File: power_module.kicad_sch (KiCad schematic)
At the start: 0 parts

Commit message: schematic: place BMS subcircuit components
25 components placed (no wires yet) in the BMS subcircuit:
  U1   BQ7692003 BMS chip (TSSOP-20)
  BT1-3  three 18650 cells stacked at x=175
  R1-4   cell-tap resistors (100 Ω) for VC0..VC3
  C1-4   cell-tap RC-filter caps (1 nF)
  Q1     dual N-channel MOSFET (FDS9926A symbol; will swap value
         to C353066 in the LCSC pass) for CHG + DSG protection
  R5     0.005 Ω current-sense shunt
  C5     1 µF cap on CAP1 (cell-balance bootstrap)
  C6/C7  REGOUT bypass (1 µF + 100 nF)
  C8/C9  BAT decoupling (10 µF + 100 nF)
  R6-8   I²C SDA/SCL + ALERT pull-ups (10 kΩ)
  R9     NTC bias (10 kΩ)
  TH1    10 kΩ NTC thermistor on TS1
  SW1    user-on/off tactile switch (placeholder; will be wired to
         BMS shutdown via small transistor in a later pass)

Placement was scripted via DynamicSymbolLoader directly rather than
going through 25 sequential MCP calls — same underlying code path,
much faster, and explicitly sequential to dodge the parallel-write
race we saw earlier today.

Component positions are approximately correct but support caps and
pull-up resistors overlap visually; will be cleaned up during wiring.

Wires + footprints + LCSC properties to follow in subsequent commits.

Co-Authored-By: Claude Opus 4.7 <noreply@anthropic.com>
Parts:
- added BT1, BT2, BT3: 18650, symbol Device:Battery_Cell
- added C1, C2, C3, C4: 1nF, symbol Device:C
- added C5, C6: 1uF, symbol Device:C
- added C7, C9: 100nF, symbol Device:C
- added C8: 10uF, symbol Device:C
- added Q1: DUAL_N_FET, symbol Transistor_FET:FDS9926A
- added R1, R2, R3, R4: 100, symbol Device:R
- added R5: 0.005, symbol Device:R
- added R6, R7, R8, R9: 10k, symbol Device:R
- added SW1: OFF, symbol Switch:SW_Push
- added TH1: NTC_10k, symbol Device:Thermistor_NTC
- added U1: BQ7692003, Package_SO:TSSOP-20_4.4x6.5mm_P0.65mm, symbol Battery_Management:BQ76920PW
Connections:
- new net: Q1.7 (D1), Q1.8 (D1)

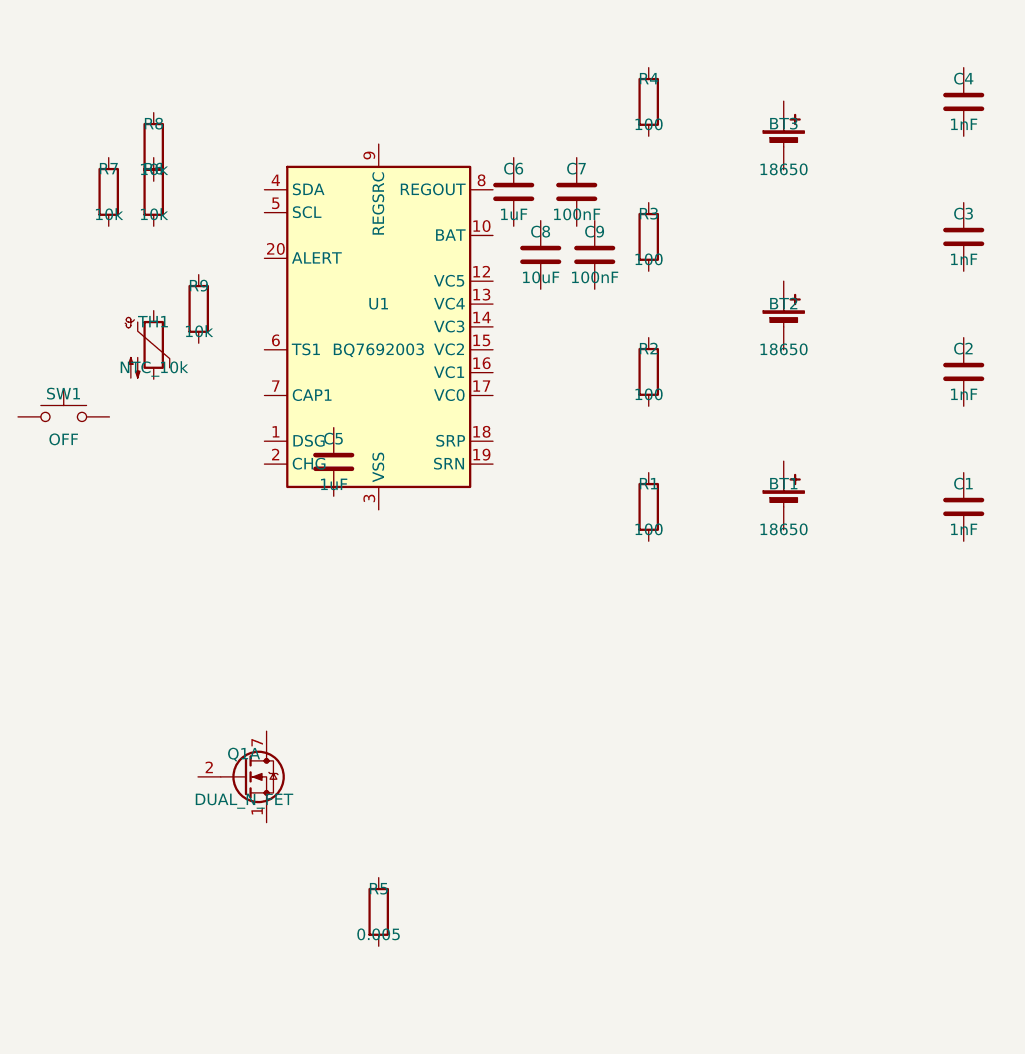
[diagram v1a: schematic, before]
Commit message: schematic: wire BMS subcircuit (cell stack, taps, FETs, signals)
All BMS-side connectivity in place via local net labels:
- Cell stack: BAT+ / CELL2_TOP / CELL1_TOP / BAT-
- Cell taps: VC0..VC3 with R1-R4 + RC caps C1-C4 (3S jumpers tie
  VC4=VC5=VC3 at the BMS pins, post-filter resistor)
- Protection FETs Q1: dual N-FET in back-to-back (drains tied =
  FET_MID, sources to BAT- and SRP, gates to BMS_DSG/BMS_CHG).
  Added Q1 unit 2 (FDS9926A symbol is multi-unit; only unit 1 was
  placed previously).
- Sense resistor R5: SRP at top, GND at bottom = U1.SRN = U1.VSS.
- Support passives: REGOUT (C6/C7), BAT/REGSRC (C8/C9 on BAT+),
  CAP1 (C5).
- Signals: SDA/SCL/ALERT pull-ups to REGOUT (R6/R7/R8); TS1
  thermistor divider (R9 + TH1 to GND).
- PWR_FLAG on BAT+ and GND so ERC accepts the cell stack as a
  power source.
- U1.NC (pin 11) marked no_connect.

ERC clean except for SW1 pins 1/2 (intentional — finalised in
integration step per NOTES.md).

Schematic file reformatted with consistent S-expression indentation
so future diffs stay readable.

Co-Authored-By: Claude Opus 4.7 <noreply@anthropic.com>
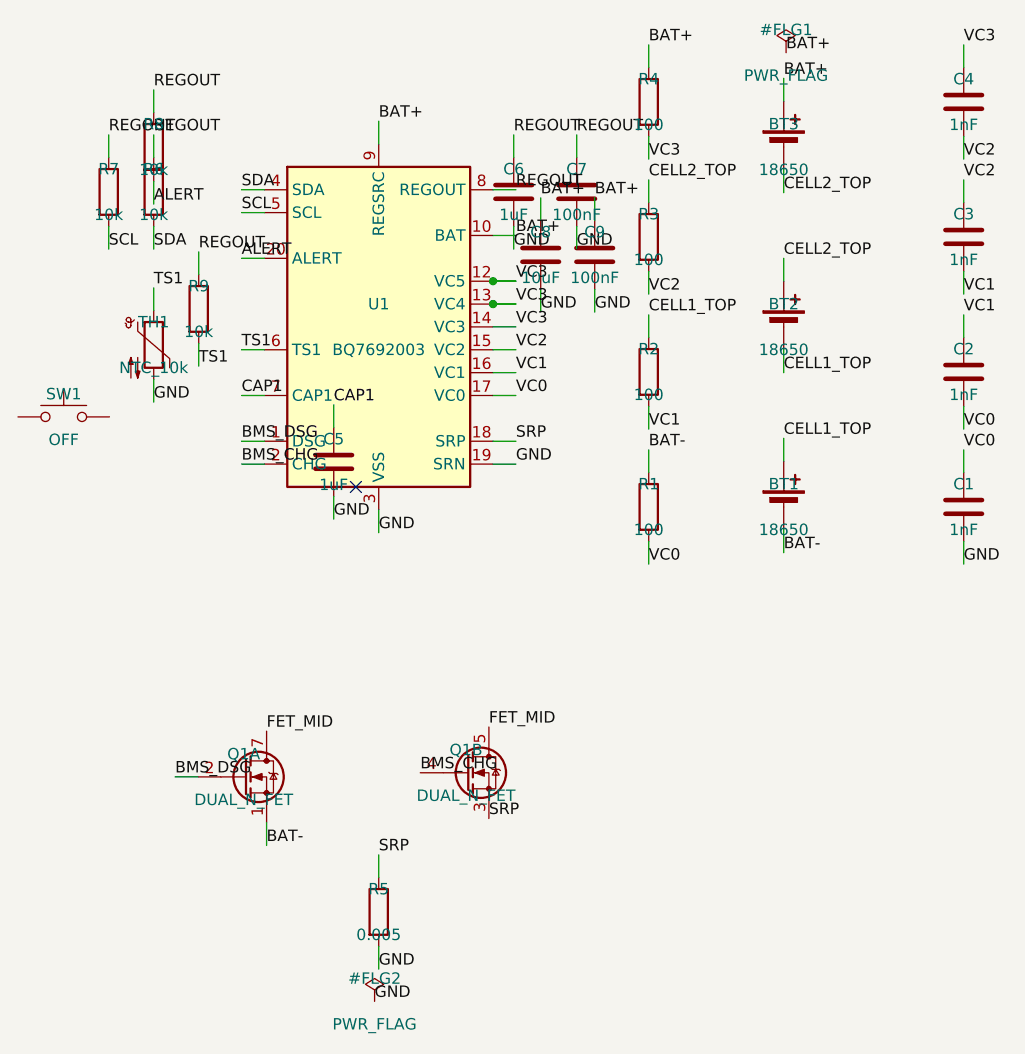
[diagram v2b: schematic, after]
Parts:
- added unit 2 of Q1
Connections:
- net VC2: now reaches C3.1
- net VC2: now also C4.2, R3.2, U1.15 (VC2)
- net VC1: now reaches C3.2
- net VC1: now also C2.1, R2.2, U1.16 (VC1)
- net REGOUT: now reaches R9.1
- net REGOUT: now also C6.1, C7.1, R6.1, R7.1, R8.1, U1.8 (REGOUT)
- net TS1: now reaches R9.2
- net TS1: now also TH1.1, U1.6 (TS1)
- net SDA: now reaches R6.2
- net SDA: now also U1.4 (SDA)
- net GND: now reaches C7.2
- net GND: now also C1.2, C5.2, C6.2, C8.2, C9.2, R5.2, TH1.2, U1.19 (SRN), U1.3 (VSS)
- net CAP1: now reaches C5.1
- net CAP1: now also U1.7 (CAP1)
- net BMS_DSG: now reaches U1.1 (DSG)
- net BMS_DSG: now also Q1.2 (G1)
- net BAT+: now reaches U1.10 (BAT)
- net BAT+: now also BT3.1 (+), C8.1, C9.1, R4.1, U1.9 (REGSRC)
- net VC3: now reaches U1.12 (VC5)
- net VC3: now also C4.1, R4.2, U1.13 (VC4), U1.14 (VC3)
- net VC0: now reaches U1.17 (VC0)
- net VC0: now also C1.1, C2.2, R1.2
- net SRP: now reaches U1.18 (SRP)
- net SRP: now also R5.1, Q1.3 (S2)
- net BMS_CHG: now reaches U1.2 (CHG)
- net BMS_CHG: now also Q1.4 (G2)
- net ALERT: now reaches U1.20 (ALERT)
- net ALERT: now also R8.2
- net SCL: now reaches U1.5 (SCL)
- net SCL: now also R7.2
- net CELL2_TOP: now reaches R3.1
- net CELL2_TOP: now also BT2.1 (+), BT3.2 (-)
- net BAT-: now reaches Q1.1 (S1)
- net BAT-: now also BT1.2 (-), R1.1
- net FET_MID: now reaches Q1.7 (D1), Q1.8 (D1)
- net FET_MID: now also Q1.5 (D2), Q1.6 (D2)
- net CELL1_TOP: now reaches BT1.1 (+)
- net CELL1_TOP: now also BT2.2 (-), R2.1
- no-connect marks 0 -> 1

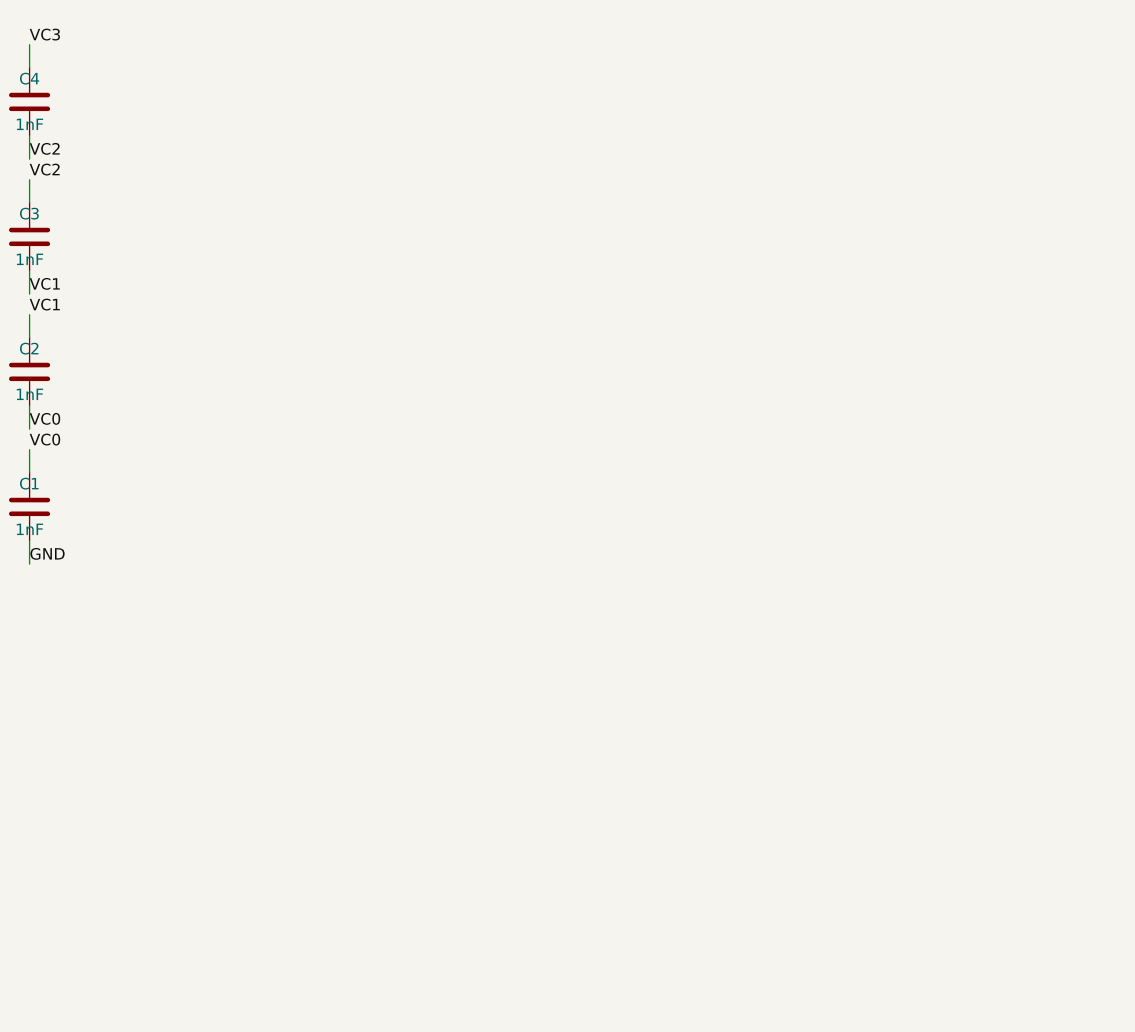
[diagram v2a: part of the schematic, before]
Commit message: schematic: add charger subcircuit (USB-C PD + BQ24650 sync buck)
22 components placed and wired:
- USB-C PowerOnly_24P receptacle (J1) → CH224K (U2) PD sink controller
  (configured for 20V request: CFG2/CFG3 to GND, CFG1 pulled to VDD via R16)
- CH224K VBUS → BQ24650 (U3) input
- BQ24650 sync buck: HIDRV/LODRV → Q2 dual N-FET (FDS9926A symbol;
  C353066 substitute at LCSC step), drains tied at PH/SW node, BTST
  bootstrap cap C12, REGN gate-drive cap C13, VREF bypass C14.
- Inductor L1 (6.8 µH) between PH and inductor-output node.
- Charger sense resistor R10 (10 mΩ) between SRP and BAT+ output;
  C15 output cap.
- VFB divider R14/R13 (100k / 20k) sets 12.6V regulation
  (VFB = 2.1V × 6 = 12.6V).
- TS divider R11/R12 (10k/10k) ties TS to mid-VREF for "no NTC" mode.
- TERM_EN, MPPSET tied to VREF (charge termination on, MPP off).
- Status LED D1 (green) with R15 current limit between USB_VBUS and
  STAT1 (open-collector pulls low when active).
- PWR_FLAG #FLG3 on USB_VBUS so ERC accepts the USB cable as the
  power source for VCC.
- Unused pins NC: U2.DP, U2.DM, U2.PG, U3.STAT2.

Naming: charger output (BQ24650.SRN) is named BAT+ so it joins the
BMS BAT+ net during integration; charger SRP is `CHG_OUT`.

ERC: 2 errors remain (SW1 placeholder pins from BMS subcircuit,
intentional). 1 warning about L_Bourns_SRR1280 footprint not found
locally — will pick a generic SMD inductor footprint at LCSC step.

Note on tooling: MCP `connect_pins` failed for every pin on the new
components even though `get_schematic_pin_locations` resolved them
correctly. Suspected stale in-memory schematic cache. Worked around
by calling `WireManager.add_label` directly via Python script. Logged
to mcp_server_issues.md.

Co-Authored-By: Claude Opus 4.7 <noreply@anthropic.com>
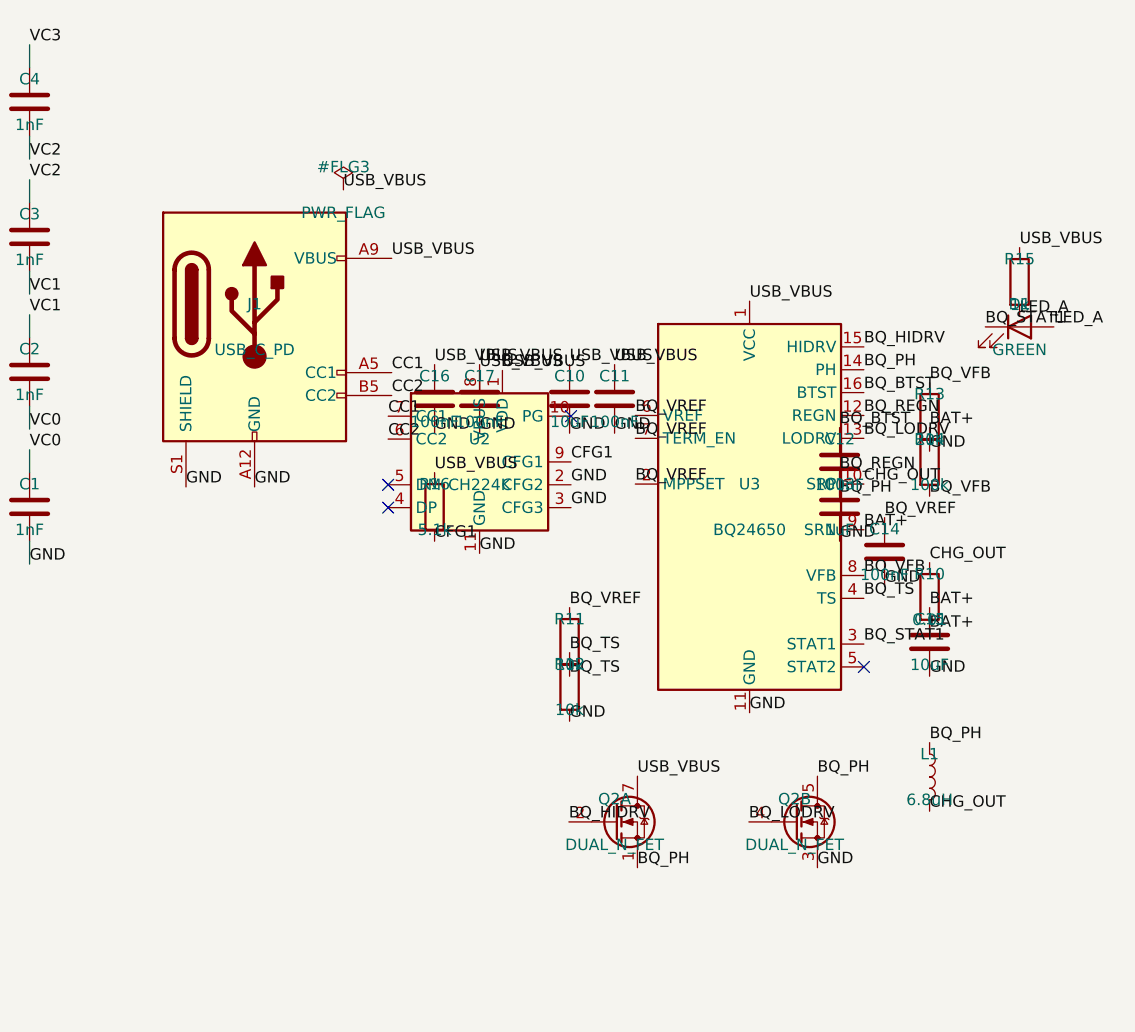
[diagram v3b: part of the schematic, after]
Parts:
- added C10, C15: 10uF, symbol Device:C
- added C11, C12, C14, C16, C17: 100nF, symbol Device:C
- added C13: 1uF, symbol Device:C
- added D1: GREEN, LED_SMD:LED_0805_2012Metric, symbol Device:LED
- added J1: USB_C_PD, Connector_USB:USB_C_Receptacle_HRO_TYPE-C-31-M-12, symbol Connector:USB_C_Receptacle_PowerOnly_24P
- added L1: 6.8uH, Inductor_SMD:L_Bourns_SRR1280, symbol Device:L
- added Q2: DUAL_N_FET, symbol Transistor_FET:FDS9926A
- added R10: 0.01, Resistor_SMD:R_2512_6332Metric, symbol Device:R
- added R11, R12: 10k, symbol Device:R
- added R13: 20k, symbol Device:R
- added R14: 100k, symbol Device:R
- added R15: 1k, symbol Device:R
- added R16: 5.1k, symbol Device:R
- added U2: CH224K, Package_SO:SSOP-10-1EP_3.9x4.9mm_P1mm_EP2.1x3.3mm, symbol Interface_USB:CH224K
- added U3: BQ24650, Package_DFN_QFN:Texas_RVA_VQFN-16-1EP_3.5x3.5mm_P0.5mm_EP2.14x2.14mm_ThermalVias, symbol Battery_Management:BQ24650
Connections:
- net BAT+: now also C15.1, R10.2, R14.1, U3.9 (SRN)
- net GND: now also C10.2, C11.2, C13.2, C14.2, C15.2, C16.2, C17.2, J1.A1 (GND), J1.A12 (GND), J1.B1 (GND), J1.B12 (GND), J1.S1 (SHIELD), Q2.3 (S2), R12.2, R13.2, U2.11 (GND), U2.2 (CFG2), U2.3 (CFG3), U3.11 (GND), U3.17 (GND)
- new net BQ_BTST: C12.1, U3.16 (BTST)
- new net BQ_HIDRV: Q2.2 (G1), U3.15 (HIDRV)
- new net BQ_LODRV: Q2.4 (G2), U3.13 (LODRV)
- new net BQ_PH: C12.2, L1.1, Q2.1 (S1), Q2.5 (D2), Q2.6 (D2), U3.14 (PH)
- new net BQ_REGN: C13.1, U3.12 (REGN)
- new net BQ_STAT1: D1.1 (K), U3.3 (STAT1)
- new net BQ_TS: R11.2, R12.1, U3.4 (TS)
- new net BQ_VFB: R13.1, R14.2, U3.8 (VFB)
- new net BQ_VREF: C14.1, R11.1, U3.2 (MPPSET), U3.6 (VREF), U3.7 (TERM_EN)
- new net CC1: J1.A5 (CC1), U2.7 (CC1)
- new net CC2: J1.B5 (CC2), U2.6 (CC2)
- new net CFG1: R16.2, U2.9 (CFG1)
- new net CHG_OUT: L1.2, R10.1, U3.10 (SRP)
- new net LED_A: D1.2 (A), R15.2
- new net USB_VBUS: C10.1, C11.1, C16.1, C17.1, J1.A4 (VBUS), J1.A9 (VBUS), J1.B4 (VBUS), J1.B9 (VBUS), Q2.7 (D1), Q2.8 (D1), R15.1, R16.1, U2.1 (VDD), U2.8 (VBUS), U3.1 (VCC)
- no-connect marks 1 -> 5
